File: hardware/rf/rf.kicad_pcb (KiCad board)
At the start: 2 copper layers, 0 parts

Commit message: Added BGT24 module castellation footprint, 3d model for 40MHz XO. Edits to schematic and pinouts based on layout of module. Initial parts placement and routing complete.
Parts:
- added C1: 100n, Capacitor_SMD:C_0201_0603Metric, F.Cu at (159.4, 91.6)
- added C10: 10p, Capacitor_SMD:C_0402_1005Metric, F.Cu at (155.4, 93.3)
- added C11: 10p, Capacitor_SMD:C_0402_1005Metric, F.Cu at (157.5, 93.3)
- added C12: 10n, Capacitor_SMD:C_0201_0603Metric, F.Cu at (163.4, 103.7)
- added C13: 2.2n, Capacitor_SMD:C_0201_0603Metric, F.Cu at (152.9, 91.3)
- added C14: 4.7u, Capacitor_SMD:C_0603_1608Metric, F.Cu at (165.7, 104.1)
- added C15: 33n, Capacitor_SMD:C_0201_0603Metric, F.Cu at (152.1, 91.3)
- added C16: ~, Capacitor_SMD:C_0201_0603Metric, F.Cu at (149.8, 90.6)
- added C17: 1n, Capacitor_SMD:C_0201_0603Metric, F.Cu at (140.3, 100.8)
- added C18: 1n, Capacitor_SMD:C_0201_0603Metric, F.Cu at (140.3, 92.8)
- added C19: 4.7u, Capacitor_SMD:C_0603_1608Metric, F.Cu at (161.8, 107.6)
- added C2: 100n, Capacitor_SMD:C_0201_0603Metric, F.Cu at (152.6, 88.2)
- added C20: 1n, Capacitor_SMD:C_0201_0603Metric, F.Cu at (150.8, 85.7)
- added C21: 10n, Capacitor_SMD:C_0201_0603Metric, F.Cu at (162.4, 106.1)
- added C22: DC BLK, bloop:DC_Block, F.Cu at (156.5, 96.7)
- added C22: DC BLK, bloop:DC_Block, F.Cu at (136.5, 89.8)
- added C23: DC BLK, bloop:DC_Block, F.Cu at (136.5, 104.5)
- added C24: 100n, Capacitor_SMD:C_0201_0603Metric, F.Cu at (140.3, 101.6)
- added C25: 10n, Capacitor_SMD:C_0201_0603Metric, F.Cu at (140.3, 93.5)
- added C3: 100n, Capacitor_SMD:C_0201_0603Metric, F.Cu at (152.6, 87.4)
- added C4: 100n, Capacitor_SMD:C_0201_0603Metric, F.Cu at (152.5, 90.1)
- added C5: 100n, Capacitor_SMD:C_0201_0603Metric, F.Cu at (165.2, 88.5)
- added C6: 100n, Capacitor_SMD:C_0201_0603Metric, F.Cu at (159.4, 92.4)
- added C7: 0.1u, Capacitor_SMD:C_0201_0603Metric, F.Cu at (159.4, 89.3)
- added C8: 0.1u, Capacitor_SMD:C_0201_0603Metric, F.Cu at (159.4, 90.1)
- added C9: 100n, Capacitor_SMD:C_0201_0603Metric, F.Cu at (159.4, 90.8)
- added FB1: Ferrite_Bead, Inductor_SMD:L_0402_1005Metric, F.Cu at (161.0, 101.6)
- added FB2: Ferrite_Bead, Inductor_SMD:L_0402_1005Metric, F.Cu at (161.3, 103.6)
- added FB3: Ferrite_Bead, Inductor_SMD:L_0402_1005Metric, F.Cu at (161.4, 104.9)
- added FL1: LPF_35GHz, bloop:35GHz_LPF, F.Cu at (154.2, 96.7)
- added J1: BGT24_Module_Castellations, bloop:BGT24_Module_Castellations, F.Cu at (166.9, 109.9)
- added J2: SMP, bloop:0734153320, F.Cu at (164.3, 96.7)
- added J3: SMP, bloop:0734153320, F.Cu at (142.7, 88.3)
- added J4: SMP, bloop:0734153320, F.Cu at (142.7, 106.1)
- added R10: 100, Capacitor_SMD:C_0201_0603Metric, F.Cu at (150.8, 86.5)
- added R2: 51, Capacitor_SMD:C_0201_0603Metric, F.Cu at (160.7, 89.7)
- added R4: 51, Capacitor_SMD:C_0201_0603Metric, F.Cu at (159.4, 88.5)
- added R5: 10k, Capacitor_SMD:C_0201_0603Metric, F.Cu at (162.1, 86.3)
- added R6: 51, Capacitor_SMD:C_0402_1005Metric, F.Cu at (159.5, 94.1)
- added R7: 120, Capacitor_SMD:C_0201_0603Metric, F.Cu at (151.0, 90.2)
- added R8: 820, Capacitor_SMD:C_0201_0603Metric, F.Cu at (151.0, 90.9)
- added U1: ECS-2520S33-400, bloop:Crystal_SMD_2520-4Pin_2.5x2.0mm, F.Cu at (163.0, 88.5)
- added U2: LMX2491, Package_DFN_QFN:VQFN-24-1EP_4x4mm_P0.5mm_EP2.45x2.45mm_ThermalVias, F.Cu at (155.9, 89.7)
- added U3: BGT24MTR12, bloop:BGT24MTR12, F.Cu at (142.7, 97.2)
- added WLK1: WILK_24_GHZ, bloop:Wilk_AWR_Mod, F.Cu at (152.0, 96.7)
- added ~: LOGO, bloop:bloop_logo_text_silkandcopper, F.Cu at (154.8, 104.4)
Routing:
- net /SPI_CLK: track 0.00 -> 46.3 mm, vias 0 -> 2
- net /SPI_MOSI: track 0.00 -> 31.8 mm, vias 0 -> 2
- net /PLL_MUX: track 0.00 -> 30.6 mm, vias 0 -> 1
- net /PLL_TRIG1: track 0.00 -> 26.9 mm, vias 0 -> 1
- net GNDRF: track 0.00 -> 19.6 mm
- net /IF2_I-: track 0.00 -> 16.9 mm, vias 0 -> 1
- net /IF2_I+: track 0.00 -> 16.9 mm, vias 0 -> 1
- net /~SPI_BGT24_CS: track 0.00 -> 16.8 mm
- net /IF1_I-: track 0.00 -> 16.4 mm, vias 0 -> 1
- net /IF1_I+: track 0.00 -> 16.4 mm, vias 0 -> 1
- net /IF1_Q-: track 0.00 -> 15.1 mm, vias 0 -> 1
- net /IF1_Q+: track 0.00 -> 15.1 mm, vias 0 -> 1
- net /IF2_Q-: track 0.00 -> 14.8 mm, vias 0 -> 1
- net /IF2_Q+: track 0.00 -> 14.8 mm, vias 0 -> 1
- net Net-(R10-Pad2): track 0.00 -> 11.7 mm, vias 0 -> 2
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- added copper zone on B.Cu, net GND
- added copper zone on F.Cu, net GNDRF
- added copper zone on In1.Cu, net GNDRF
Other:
- board outline added: 33.5 x 25.4 mm
- copper layers 2 -> 4
- net class 50ohm_24GHz: trace_width 0.25 -> 0.5334

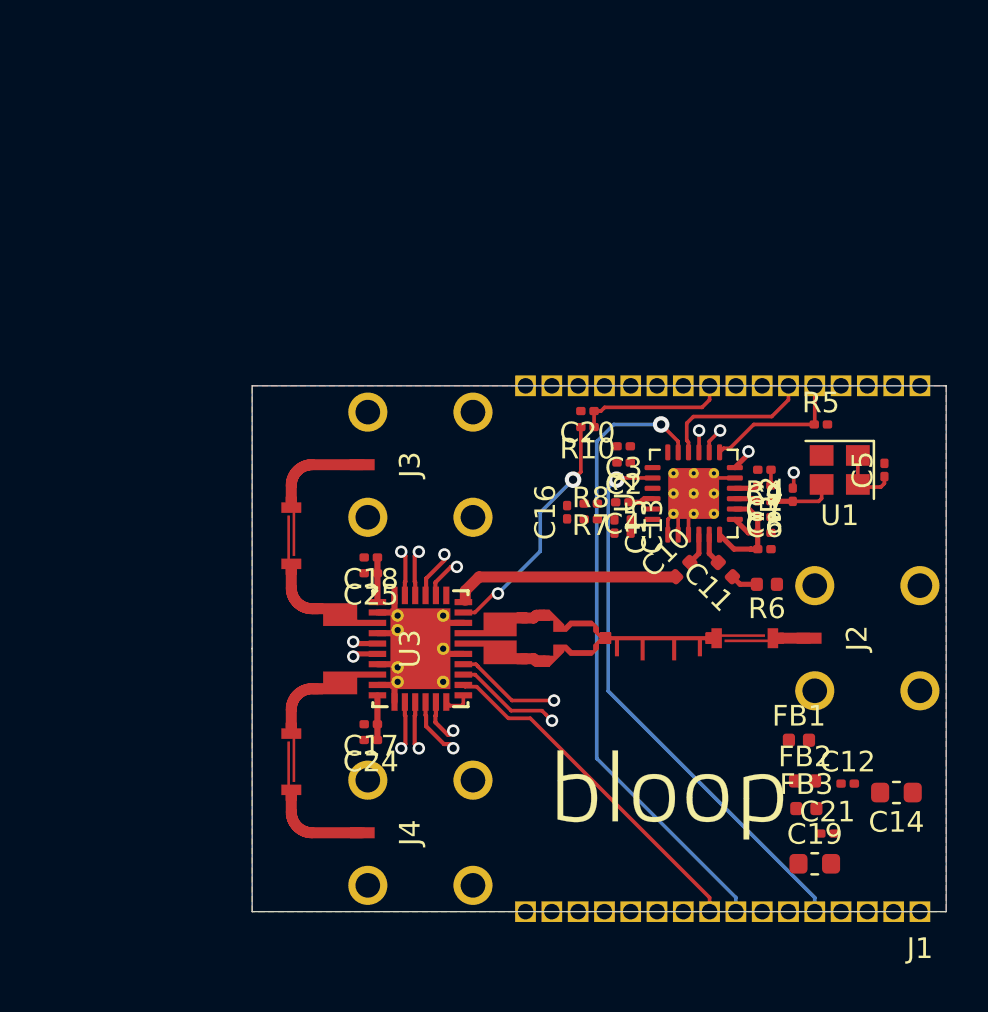
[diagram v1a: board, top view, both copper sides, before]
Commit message: Added 85305-0232 footprint for SMT SMP connector
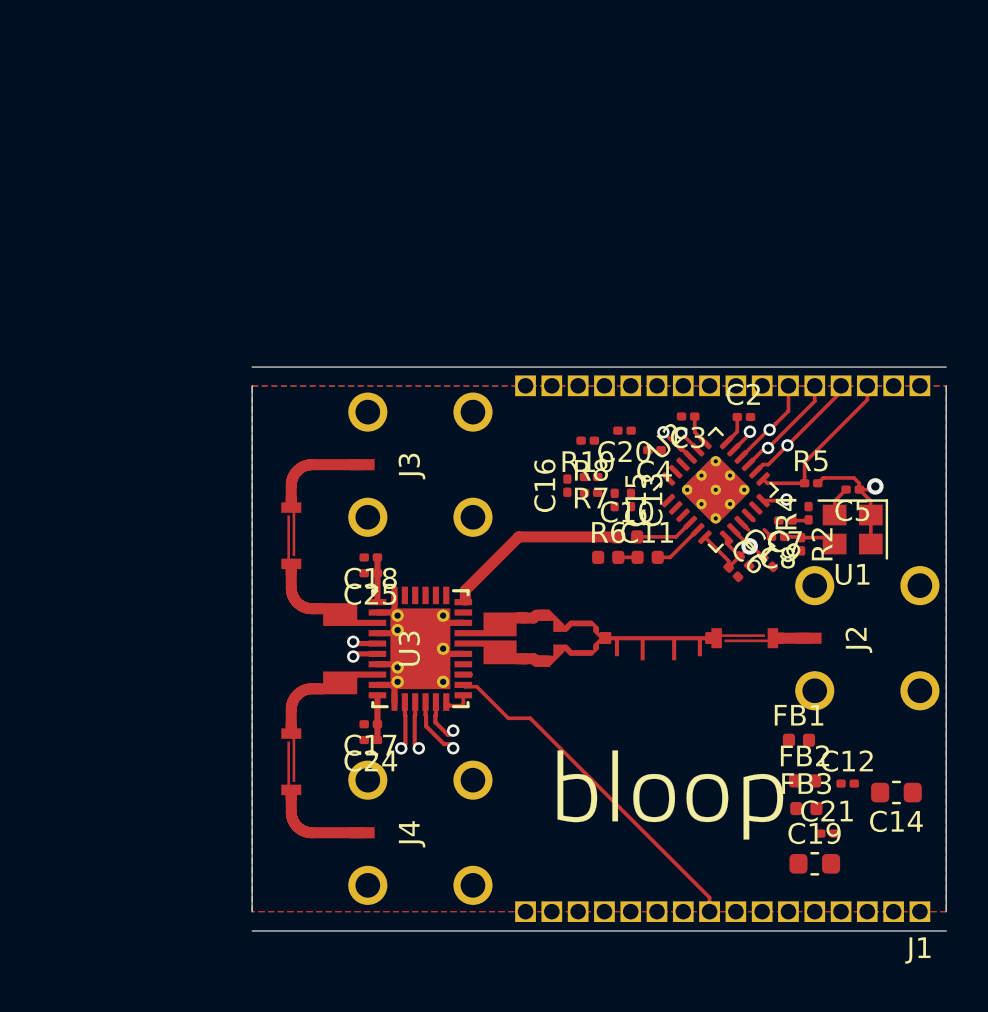
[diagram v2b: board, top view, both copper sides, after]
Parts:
- moved R6 7.77 mm to (151.8, 92.8), turned to 0 degrees
- moved C2 6.21 mm to (158.4, 86.0), turned to 0 degrees
- moved C11 3.80 mm to (153.7, 92.8), turned to 0 degrees
- moved C3 3.43 mm to (155.7, 86.0)
- moved C10 3.12 mm to (152.7, 91.8), turned to 0 degrees
- moved R4 2.99 mm to (161.5, 90.6), turned to 90 degrees
- moved C4 2.96 mm to (154.1, 87.6)
- moved U1 2.95 mm to (163.6, 91.4)
- moved R5 2.88 mm to (161.6, 89.2)
- moved R2 2.43 mm to (161.1, 92.1), turned to 270 degrees
- moved C9 2.18 mm to (159.5, 93.0), turned to 315 degrees
- moved C20 2.03 mm to (152.6, 86.6)
- moved C7 1.98 mm to (160.4, 91.0)
- moved C6 1.86 mm to (157.9, 93.5), turned to 315 degrees
- moved C8 1.84 mm to (160.0, 91.8)
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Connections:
- J1 pad 28: /SPI_CE_PLL -> /SPI_MOSI
- J1 pad 29: /SPI_MOSI -> /SPI_CLK
- J1 pad 30: /SPI_CLK -> /SPI_CE_PLL
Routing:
- net /SPI_CLK: track 46.3 -> 6.39 mm, vias 2 -> 1
- net /PLL_MUX: track 30.6 -> 1.19 mm
- net /SPI_MOSI: track 31.8 -> 5.43 mm, vias 2 -> 1
- net /PLL_TRIG1: track 26.9 -> 1.12 mm
- net /IF1_I-: track 16.4 -> 0.00 mm, vias 1 -> 0
- net /IF1_I+: track 16.4 -> 0.00 mm, vias 1 -> 0
- net /IF1_Q-: track 15.1 -> 0.00 mm, vias 1 -> 0
- net /IF1_Q+: track 15.1 -> 0.00 mm, vias 1 -> 0
- net Net-(R10-Pad2): track 11.7 -> 0.00 mm, vias 2 -> 0
- net GNDRF: track 19.6 -> 10.4 mm
- net /BGT24_ANA: track 7.26 -> 0.00 mm
- net +3V3_PLL: track 10.7 -> 15.7 mm, vias 0 -> 2
- net /PLL_LE: track 7.50 -> 4.42 mm, vias 0 -> 1
- net /PLL_DIV16: track 11.1 -> 9.06 mm
- net /PLL_TRIG2: track 0.00 -> 1.80 mm, vias 0 -> 1
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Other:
- board size 33.5 x 25.4 mm -> 33.5 x 27.2 mm

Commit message: Replaced TH SMP connectors with SMT
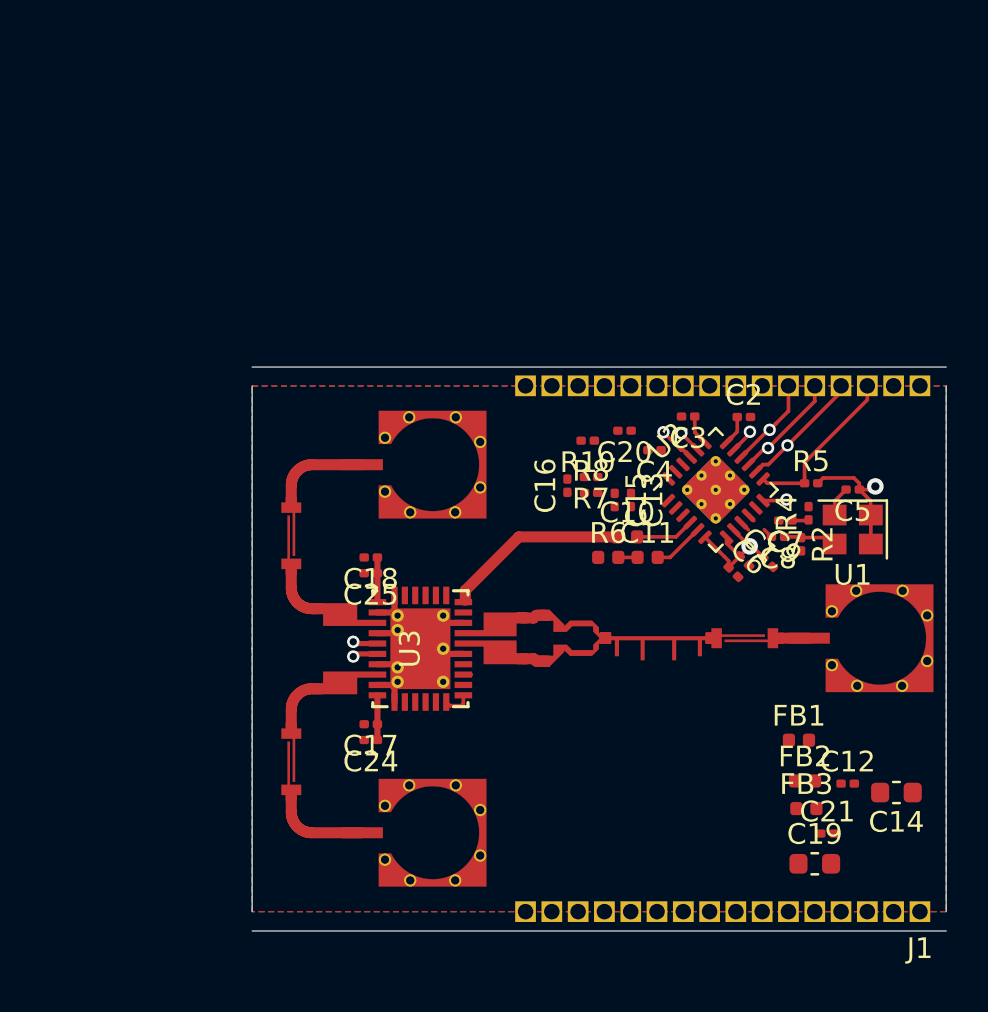
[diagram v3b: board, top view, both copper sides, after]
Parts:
- removed ~: LOGO, bloop:bloop_logo_text_silkandcopper
- J2, J3, J4: footprint bloop:0734153320 -> bloop:85305-0232
- moved J2 0.59 mm to (164.9, 96.7), turned to 0 degrees
- moved J3 0.59 mm to (143.3, 88.3), turned to 0 degrees
- moved J4 0.59 mm to (143.3, 106.1), turned to 0 degrees
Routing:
- net /IF2_I-: track 16.9 -> 0.00 mm, vias 1 -> 0
- net /IF2_I+: track 16.9 -> 0.00 mm, vias 1 -> 0
- net /~SPI_BGT24_CS: track 16.8 -> 0.00 mm
- net /IF2_Q-: track 14.8 -> 0.00 mm, vias 1 -> 0
- net /IF2_Q+: track 14.8 -> 0.00 mm, vias 1 -> 0
- net Net-(FL1-Pad1): track 1.40 -> 0.00 mm
- net Net-(C22-Pad2): track 2.75 -> 4.15 mm

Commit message: Add 30 mil mask; update schematic for connector orientation
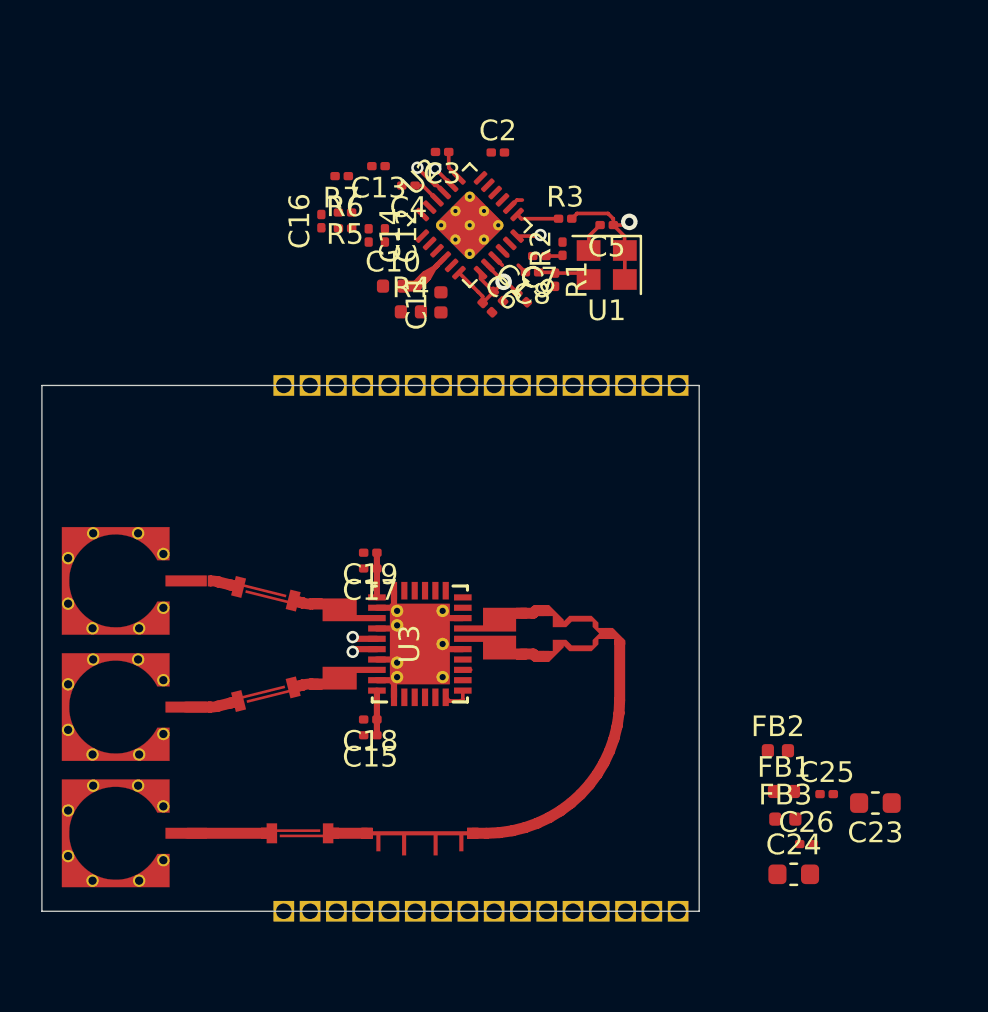
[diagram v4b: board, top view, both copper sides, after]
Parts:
- removed the C15 at (152.1, 90.0)
- removed the C19 at (161.8, 107.6)
- removed the C22 at (156.5, 96.7)
- removed the C22 at (136.5, 89.8)
- removed the C23 at (136.5, 104.5)
- removed R10: 100, Capacitor_SMD:C_0201_0603Metric
- removed R8: 820, Capacitor_SMD:C_0201_0603Metric
- added ?: , , F.Cu at (132.6, 100.0)
- added ?: , , F.Cu at (137.5, 98.9)
- added ?: , , F.Cu at (133.0, 93.9)
- added ?: , , F.Cu at (137.0, 95.0)
- added ?: , , F.Cu at (152.4, 96.9)
- added ?: , , F.Cu at (143.5, 78.7)
- added C12: 2.2n, Capacitor_SMD:C_0201_0603Metric, F.Cu at (141.0, 77.2)
- added C14: 33n, Capacitor_SMD:C_0201_0603Metric, F.Cu at (140.2, 77.2)
- added C21: DC BLK, bloop:DC_Block, F.Cu at (133.5, 99.8)
- added C22: DC BLK, bloop:DC_Block, F.Cu at (135.0, 106.1)
- added C24: 4.7u, Capacitor_SMD:C_0603_1608Metric, F.Cu at (160.8, 108.1)
- added R1: 51, Capacitor_SMD:C_0201_0603Metric, F.Cu at (149.3, 79.3)
- added R3: 10k, Capacitor_SMD:C_0201_0603Metric, F.Cu at (149.7, 76.4)
- C13: value 2.2n -> 1n
- C20: value 1n -> DC BLK; footprint Capacitor_SMD:C_0201_0603Metric -> bloop:DC_Block
- J1: moved to B.Cu
- R4: footprint Capacitor_SMD:C_0201_0603Metric -> Capacitor_SMD:C_0402_1005Metric
- R5: value 10k -> 120
- R6: value 51 -> 820; footprint Capacitor_SMD:C_0402_1005Metric -> Capacitor_SMD:C_0201_0603Metric
- R7: value 120 -> 100
- moved J2 38.1 mm to (128.0, 106.1), turned to 180 degrees
- moved J1 28.0 mm to (155.2, 84.5)
- moved R5 26.0 mm to (139.1, 76.1), turned to 180 degrees
- moved R4 21.5 mm to (142.3, 80.9), turned to 0 degrees
- moved C20 20.5 mm to (133.5, 94.1), turned to 256 degrees
- moved R6 20.4 mm to (139.1, 76.9)
- moved C13 20.2 mm to (140.7, 73.9), turned to 180 degrees
- moved R7 18.9 mm to (138.9, 74.3)
- moved R2 18.4 mm to (149.6, 77.8), turned to 90 degrees
- moved C1 17.5 mm to (146.5, 80.2)
- moved C16 17.5 mm to (138.0, 76.5)
- moved C2 17.5 mm to (146.5, 73.2)
- moved C3 17.5 mm to (143.8, 73.2)
- moved C4 17.5 mm to (142.2, 74.8)
- moved C5 17.5 mm to (151.7, 76.7)
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- renumbered C24 to C15, C25 to C17, C17 to C18, C18 to C19, C14 to C23, C12 to C25, C21 to C26, FB2 to FB1, FB1 to FB2
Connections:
- C13 pad 1: Net-(C13-Pad1) -> /BGT24_ANA
- C20 pad 1: /BGT24_ANA -> Net-(C20-Pad1)
- C20 pad 2: GNDRF -> Net-(C20-Pad2)
- J1 pad 1: PWR_IN -> GND
- J1 pad 11: /IF2_I- -> /IF1_I-
- J1 pad 12: /IF2_I+ -> /IF1_I+
- J1 pad 14: /IF2_Q+ -> /IF1_Q+
- J1 pad 15: /IF2_Q- -> /IF1_Q-
- J1 pad 18: /IF1_Q- -> /IF2_Q-
- J1 pad 19: /IF1_Q+ -> /IF2_Q+
- J1 pad 2: PWR_IN -> GND
- J1 pad 21: /IF1_I+ -> /IF2_I+
- J1 pad 22: /IF1_I- -> /IF2_I-
- J1 pad 24: /BGT24_ANA -> /~SPI_BGT24_CS
- J1 pad 25: /PLL_DIV_MCU -> /PLL_MUX
- J1 pad 26: GND -> /PLL_MOD
- J1 pad 27: /PLL_LE -> /PLL_TRIG2
- J1 pad 28: /SPI_MOSI -> /PLL_TRIG1
- J1 pad 29: /SPI_CLK -> GND
- J1 pad 3: GND -> /SPI_CE_PLL
- J1 pad 30: /SPI_CE_PLL -> GND
- J1 pad 31: GND -> PWR_IN
- J1 pad 32: GND -> PWR_IN
- J1 pad 4: GND -> /SPI_CLK
- J1 pad 5: /PLL_TRIG1 -> /SPI_MOSI
- J1 pad 6: /PLL_TRIG2 -> /PLL_LE
- J1 pad 7: /PLL_MOD -> GND
- J1 pad 8: /PLL_MUX -> /PLL_DIV_MCU
- J1 pad 9: /~SPI_BGT24_CS -> /BGT24_ANA
- J2 pad 1: Net-(FL1-Pad1) -> Net-(C22-Pad1)
- J3 pad 1: Net-(C22-Pad1) -> Net-(C20-Pad1)
- R2 pad 1: /40MHZ_CLK_OUT -> Net-(C7-Pad1)
- R2 pad 2: GND -> GNDRF
- R4 pad 1: Net-(C7-Pad1) -> GNDRF
- R4 pad 2: GNDRF -> Net-(C11-Pad1)
- R5 pad 1: /SPI_CE_PLL -> Net-(C14-Pad2)
- R5 pad 2: +3V3_PLL -> GNDRF
- R6 pad 1: GNDRF -> Net-(C16-Pad1)
- R6 pad 2: Net-(C11-Pad1) -> Net-(C12-Pad1)
- R7 pad 1: Net-(C15-Pad2) -> /BGT24_ANA
- R7 pad 2: GNDRF -> Net-(R7-Pad2)
- U2 pad 24: Net-(C13-Pad1) -> Net-(C12-Pad1)
- U3 pad 25: Net-(R10-Pad2) -> Net-(R7-Pad2)
- U3 pad 3: Net-(C22-Pad2) -> Net-(C20-Pad2)
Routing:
- net Net-(FL1-Pad1): track 0.00 -> 13.8 mm
- net /PLL_DIV16: track 9.06 -> 0.00 mm
- net /SPI_CE_PLL: track 8.05 -> 2.09 mm
- net /SPI_MOSI: track 5.43 -> 0.00 mm, vias 1 -> 0
- net /SPI_CLK: track 6.39 -> 1.13 mm, vias 1 -> 0
- net /PLL_LE: track 4.42 -> 0.00 mm, vias 1 -> 0
- net Net-(C21-Pad1): track 4.81 -> 1.88 mm
- net Net-(C22-Pad2): track 4.15 -> 1.62 mm
- net Net-(C11-Pad2): track 2.48 -> 0.00 mm
- net Net-(C21-Pad2): track 2.75 -> 0.28 mm
- net Net-(C10-Pad2): track 2.85 -> 1.65 mm
- net /PLL_MUX: track 1.19 -> 0.00 mm, vias 1 -> 0
- net Net-(C22-Pad1): track 4.81 -> 3.81 mm
- net Net-(C11-Pad1): track 0.94 -> 0.00 mm
- net Net-(C20-Pad1): track 0.00 -> 0.74 mm
- removed copper zone on B.Cu, net GND
- removed copper zone on F.Cu, net GNDRF
- removed copper zone on In1.Cu, net GNDRF
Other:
- board size 33.5 x 27.2 mm -> 31.8 x 25.4 mm

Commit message: Stitched in some via-bois
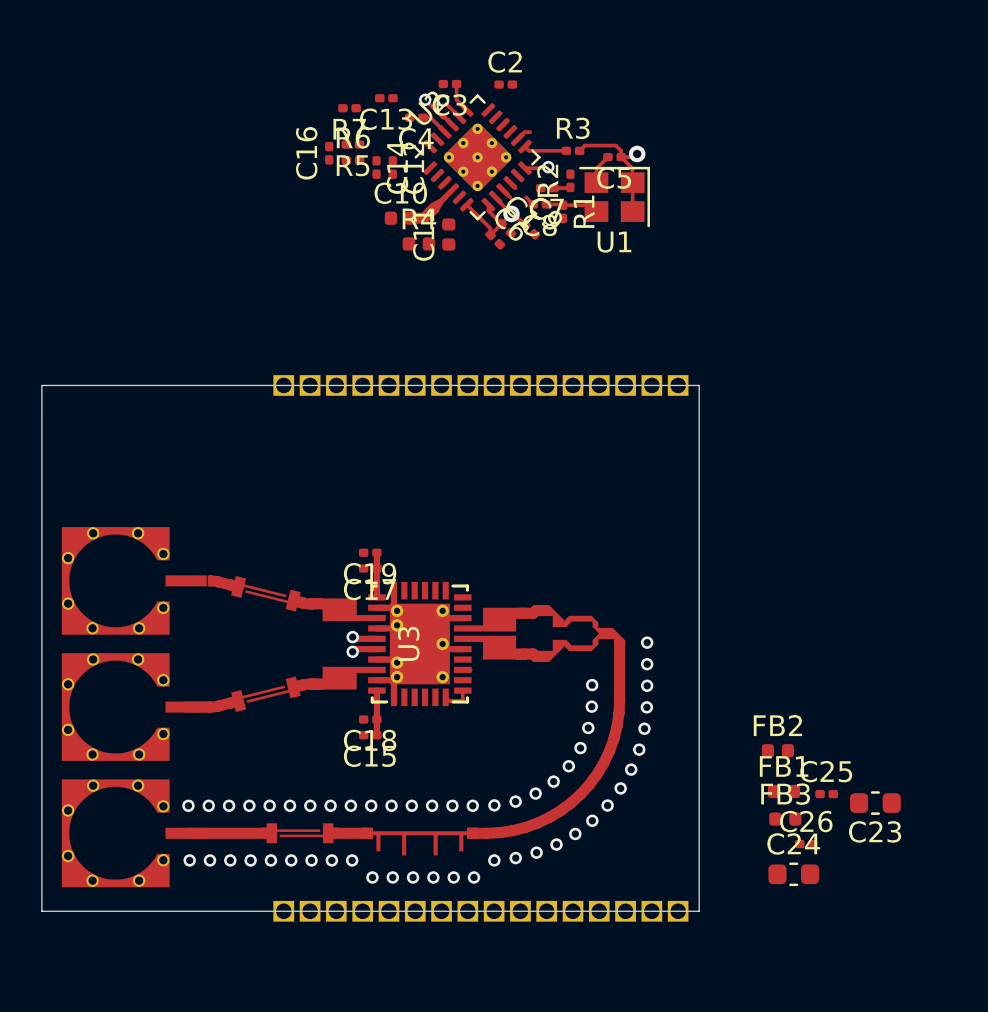
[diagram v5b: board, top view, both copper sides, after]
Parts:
- U3: value BGT24MTR12 -> VQFN-32-9
- moved C13 3.30 mm to (141.1, 70.6)
- moved R3 3.30 mm to (150.1, 73.1)
- moved R4 3.30 mm to (142.7, 77.6)
- moved C1 3.30 mm to (146.9, 76.9)
- moved C10 3.30 mm to (141.8, 76.4)
- moved C11 3.30 mm to (144.1, 77.2)
- moved C12 3.30 mm to (141.4, 73.9)
- moved C14 3.30 mm to (140.6, 73.9)
- moved C16 3.30 mm to (138.3, 73.2)
- moved C2 3.30 mm to (146.9, 69.9)
- moved C3 3.30 mm to (144.2, 69.9)
- moved C4 3.30 mm to (142.5, 71.5)
- moved C5 3.30 mm to (152.1, 73.4)
- moved C6 3.30 mm to (146.4, 77.4)
- moved C7 3.30 mm to (148.9, 74.9)
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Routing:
- net GNDRF: vias 0 -> 54
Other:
- net class Default: clearance 0.1778 -> 0.127; trace_width 0.1778 -> 0.127
- rule trace_clearance: 0.1778 -> 0.127
